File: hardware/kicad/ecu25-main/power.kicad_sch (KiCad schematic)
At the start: 25 parts, among them J1 Screw_Terminal_BATT, Q1 SQJ457EP, U1 LM5164DDA-Q1, U2 TLV75533 (500mA)

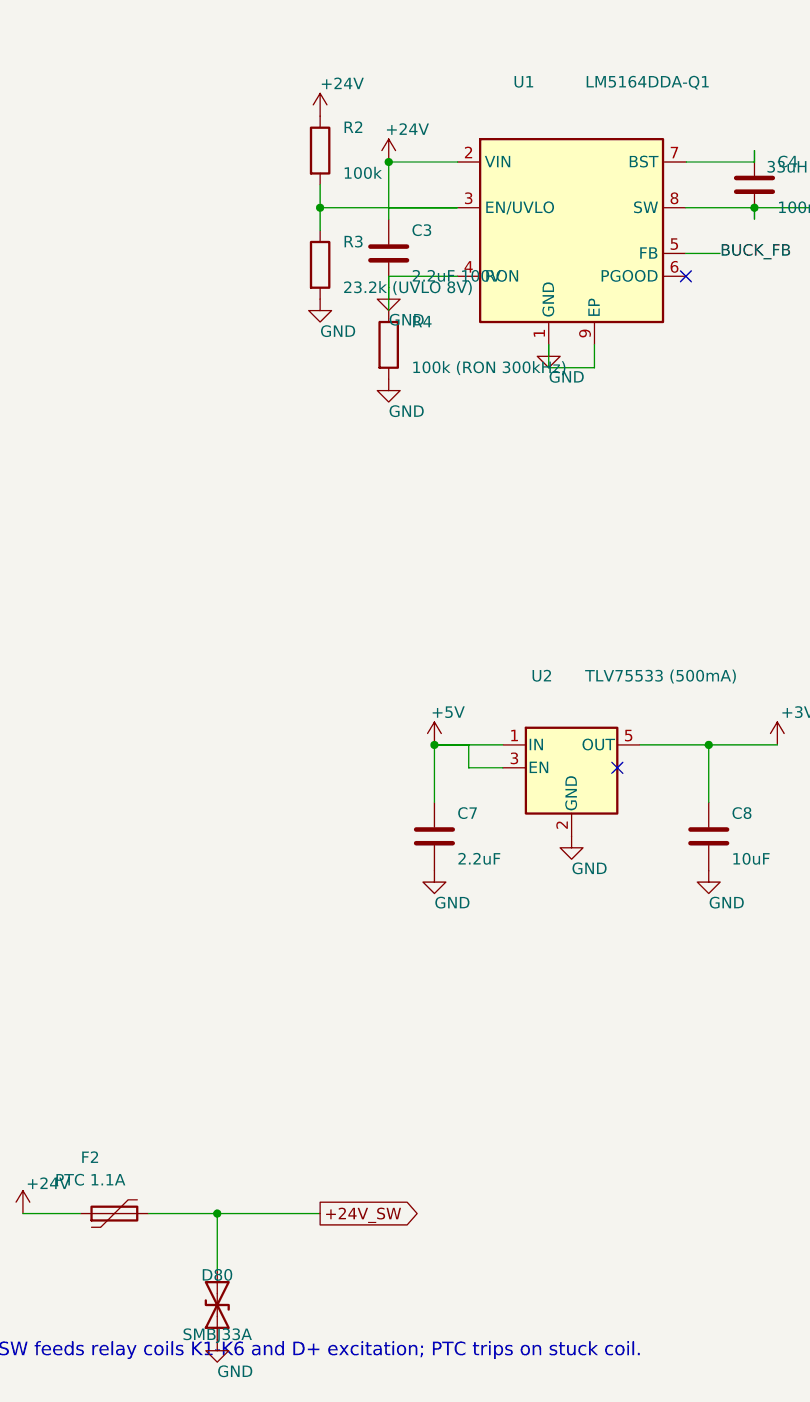
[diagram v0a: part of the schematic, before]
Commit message: Fix SME review findings: 3 critical, 6 major schematic faults
Critical:
- RON pin no longer shorted to GND (R4 moved off C3's column)
- LM2903 MPU comparator +/- inputs unmerged (separate route columns)
- Supercap charge diode D70 un-reversed (anode to +3V3)

Major:
- Buck UVLO divider restored (stray EN stub ended on C3 column = EN
  tied to +24V; stub removed)
- RS485 fail-safe bias polarity corrected (pull-up A, pull-down B)
- U8 spare op-amp unit placed and tied off (was floating on VREF die)
- Heartbeat LED DS1 un-reversed
- VREF_MID buffer dual feedback added (R93 DC path + C93 AC path)
- D80 value SMBJ33A -> SMBJ33CA (bidirectional, matches symbol)

Added netlist-level sweep check (shorted 2-pin devices, rail
membership) since the geometric tracer is blind to shorts closed
through power symbols across wire islands. Sweep: CLEAN, 0 issues.
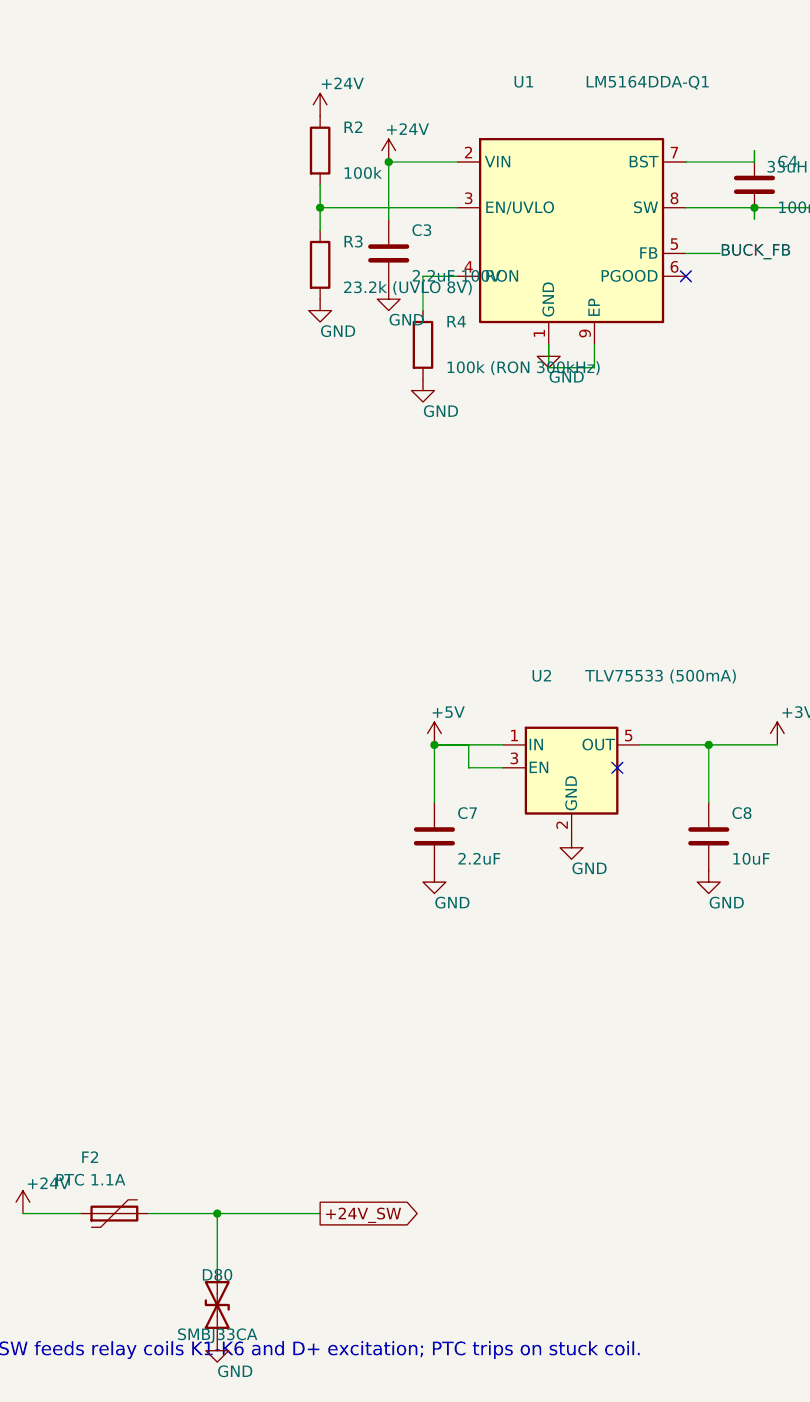
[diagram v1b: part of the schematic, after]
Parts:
- D80: value SMBJ33A -> SMBJ33CA
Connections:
- net +24V: no longer R2.2, R3.1, U1.3 (EN/UVLO)
- net GND: no longer R4.1, U1.4 (RON)
- new net: R2.2, R3.1, U1.3 (EN/UVLO)
- new net: R4.1, U1.4 (RON)

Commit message: Assign footprints to all 299 components in schematic generator
- By-ref exceptions + per-symbol defaults + value rules (wattage/voltage classes)
- Field connectors: MKDS-3 for battery/AC/CT/relay terminals, MKDS-1,5 for signal
- Q1 reverse-protection FET: Q_PMOS_GSD -> Q_PMOS_GDS + TO-252-2 (DPAK pad
  numbering 1=G 2=D 3=S; GSD variant would swap D/S in the netlist), part
  SQD50P06-15L
- Verified: all footprint files exist in KiCad 7 libs, all symbol pin numbers
  present in footprint pads, netlist sweep still clean
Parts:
- removed Q1: SQJ457EP, symbol Device:Q_PMOS_GSD
- added Q1: SQD50P06-15L, Package_TO_SOT_SMD:TO-252-2, symbol Device:Q_PMOS_GDS
- C1: footprint (none) -> Capacitor_THT:CP_Radial_D8.0mm_P3.50mm
- C2, C4, C7: footprint (none) -> Capacitor_SMD:C_0603_1608Metric
- C3, C5, C6: footprint (none) -> Capacitor_SMD:C_1210_3225Metric
- C8: footprint (none) -> Capacitor_SMD:C_0805_2012Metric
- D1: footprint (none) -> Diode_SMD:D_SMC
- D2: footprint (none) -> Diode_SMD:D_SOD-123
- D80: footprint (none) -> Diode_SMD:D_SMB
- F1: footprint (none) -> Fuse:Fuseholder_Blade_Mini_Keystone_3568
- F2: footprint (none) -> Fuse:Fuse_1812_4532Metric
- FB1: footprint (none) -> Inductor_SMD:L_0805_2012Metric
- J1: footprint (none) -> TerminalBlock_Phoenix:TerminalBlock_Phoenix_MKDS-3-2-5.08_1x02_P5.08mm_Horizontal
- L2: footprint (none) -> Inductor_SMD:L_12x12mm_H8mm
- R1, R2, R3, R4, R5, R6: footprint (none) -> Resistor_SMD:R_0603_1608Metric
- U1: footprint (none) -> Package_SO:SOIC-8-1EP_3.9x4.9mm_P1.27mm_EP2.514x3.2mm_ThermalVias
- U2: footprint (none) -> Package_TO_SOT_SMD:SOT-23-5
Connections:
- net at D1.2 (A2), F1.2: now also Q1.2 (D)
- net at D2.2 (A), R1.1: now also Q1.1 (G)
- net at D2.1 (K), FB1.1: now also Q1.3 (S)

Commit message: Fix PCB SME review findings: relay pin map, 415V clearances, terminal creepage
CRITICAL: G5LE-1 pin map — lib symbol/footprint has coil on pins 2/5, COM 1,
NO 3, NC 4; generator assumed 1/2 coil + 3/4/5 contacts, netting all six
relays dead (coil open, outputs on NC, volt-free GEN/MAINS contacts tied to
logic GND through the driver FETs). Relay sheet rewired, verified by netlist.

MAJOR fixes, all generator-side:
- Volt-free contactor pairs split off J8 onto new J15; J5/J6/J15 are 8-pole
  5.08mm blocks with only odd poles wired (10.16mm live pitch) + pad remap —
  fully-populated 400V-class blocks don't meet PD2 creepage for 415V L-L /
  unsynchronized-source spacing
- DRU rebuilt: GND no longer swept into the line class (was making the board
  unroutable), 3.0mm line class now includes the J15 contactor nets, per-chain
  1.0mm exemptions so the first 330k doesn't false-trip, netless-pad rule,
  generated-file header
- Copper-pour keepouts under J5/J6, the 330k chains, and the volt-free
  contact corridor K3/K4 -> J15
- CT burden + TVS fixed at J7; buck hot loop (C3/U1/L2/C5/C6) and input chain
  fixed in electrical order; R88 (2.6W) moved to the board edge away from
  precision analog; packer margin 0.4 -> 0.6mm
- F2 PTC now specified 60V (sees the 53V load-dump clamp while tripped)

Docs + diagrams + PDFs synced; verified: no overlaps, nothing outside
outline, odd-pole remap correct on J5/J6/J15, netlist sweep clean
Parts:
- F2: value PTC 1.1A -> PTC 1.1A 60V

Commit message: Add BOM generator + breadboard prototyping guide; fix parts found by review
New:
- gen_bom.py: builds docs/bom/ecu25-main-bom.{md,csv} from the netlist —
  300 components in 91 order lines, grouped by orderable value + package,
  with part numbers for the actives and a shared-across-sheets section
- docs/bom/breadboard-prototype.md: through-hole translation in eight blocks
  (digital input, relay driver, sender current source, VREF buffer, MPU
  comparator, CT, AC sense, comms), each with an explicit node list, a
  reference-schematic link, and a test that proves that block. Safety rules
  for the 415V sensing (not on a breadboard), CT open-circuit, grounding,
  and supply current limiting

Design corrections the BOM review reached back into:
- F2 was specified as a 60V 1812 PPTC that does not exist (the 0ZCJ0110 is
  8V/1206) -> RXEF110, 72V radial, on Fuse_Bourns_MF-RG900 (1.01mm drill for
  its 0.81mm leads)
- C1 50V -> 63V and C2 50V -> 100V: both sit on +24V, which D1 clamps to ~53V
- CT gain pairs (R51/R52, R56/R57, R64/R65) and the phase-match resistors
  (R53/R58/R66) now carry explicit 1% — 5% pairs would give up to 7% gain
  error on every current and power reading
- G5LE-1-DC24 coil is 1.44k / 400mW / 16.7mA, not 360R / 67mA: a 4x error
  that had propagated through three documents. Every sizing decision was made
  against the larger number, so all of them keep margin
- F2 also gates the four switched outputs, not just the coils — documented

Board:
- Netclasses in .kicad_pro (Battery/Power/Logic/GND/HV_AC/HV_CHAIN) with
  track widths and clearances; +3V3/+5V split into Logic because the
  LQFP-100's own pads are 0.2mm apart and cannot take a wide clearance class
- GND pour fills at the widest non-HV class, with keepouts around every NPTH
  barrel; minimum through-drill 0.2mm to match U1's library thermal vias
- Board now reports zero DRC errors (unrouted ratsnest and silk warnings
  aside), no courtyard overlaps, nothing outside the outline

Also: route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
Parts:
- C1: value 100uF 50V -> 100uF 63V; footprint Capacitor_THT:CP_Radial_D8.0mm_P3.50mm -> Capacitor_THT:CP_Radial_D10.0mm_P5.00mm
- C2: value 100nF 50V -> 100nF 100V; footprint Capacitor_SMD:C_0603_1608Metric -> Capacitor_SMD:C_0805_2012Metric
- F2: value PTC 1.1A 60V -> PTC 1.1A 72V; footprint Fuse:Fuse_1812_4532Metric -> Fuse:Fuse_Bourns_MF-RG900
